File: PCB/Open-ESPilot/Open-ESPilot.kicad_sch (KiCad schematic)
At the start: 0 parts

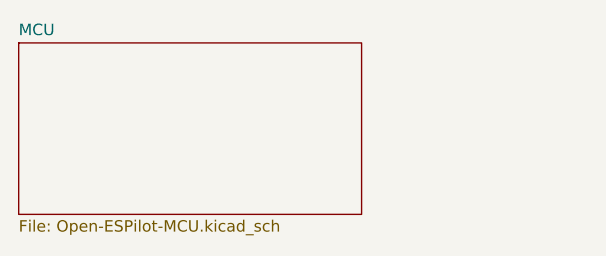
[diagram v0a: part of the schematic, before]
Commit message: Finished schematic for the ESP32S3.
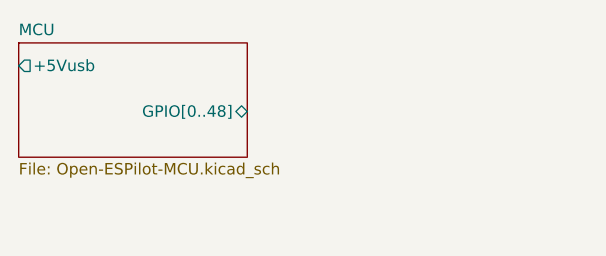
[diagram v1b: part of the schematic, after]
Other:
- sheet MCU ports: added +5Vusb, GPIO[0..48]; removed none
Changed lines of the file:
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@@
 	(sheet
 		(at 110.49 77.47)
-		(size 38.1 19.05)
+		(size 25.4 12.7)
 		(exclude_from_sim no)
 		(in_bom yes)
@@
 		)
 		(property "Sheetfile" "Open-ESPilot-MCU.kicad_sch"
-			(at 110.49 97.1046 0)
+			(at 110.49 90.7546 0)
 			(effects
 				(font
@@
 			)
 		)
+		(pin "+5Vusb" output
+			(at 110.49 80.01 180)
+			(effects
+				(font
+					(size 1.27 1.27)
+				)
+				(justify left)
+			)
+		)
+		(pin "GPIO[0..48]" bidirectional
+			(at 135.89 85.09 0)
+			(effects
+				(font
+					(size 1.27 1.27)
+				)
+				(justify right)
+			)
+		)

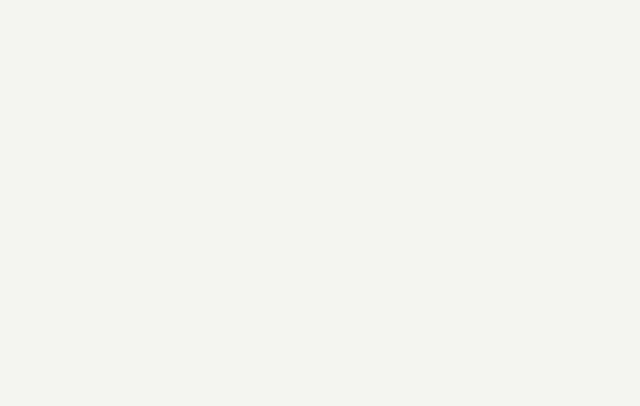
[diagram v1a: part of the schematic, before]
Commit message: Edited the MP1584 module and added Schematic and footprint of the GY-91 and implemented it to the schematic.
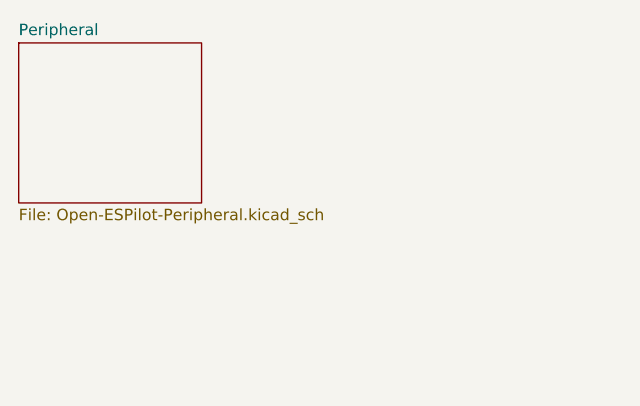
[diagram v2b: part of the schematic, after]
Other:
- added sheet Peripheral (Open-ESPilot-Peripheral.kicad_sch)
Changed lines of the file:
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@@
+		)
+	)
+	(sheet
+		(at 52.07 29.21)
+		(size 20.32 17.78)
+		(exclude_from_sim no)
+		(in_bom yes)
+		(on_board yes)
+		(dnp no)
+		(fields_autoplaced yes)
+		(stroke
+			(width 0.1524)
+			(type solid)
+		)
+		(fill
+			(color 0 0 0 0.0000)
+		)
+		(property "Sheetname" "Peripheral"
+			(at 52.07 28.4984 0)
+			(effects
+				(font
+					(size 1.27 1.27)
+				)
+				(justify left bottom)
+			)
+		)
+		(property "Sheetfile" "Open-ESPilot-Peripheral.kicad_sch"
+			(at 52.07 47.5746 0)
+			(effects
+				(font
+					(size 1.27 1.27)
+				)
+				(justify left top)
+			)
+		)
+		(instances
+			(project "Open-ESPilot"
+				(path "/2992e60d-a645-4cd7-90ae-fe72311b6bee"
+					(page "4")
+				)
+			)
 		)
 	)

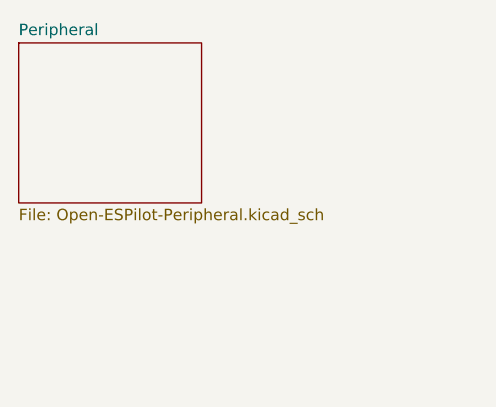
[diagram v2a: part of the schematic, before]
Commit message: Edited Pin definitions to Open ESPilot. And added the pheripherials to the schematic. Also new journal entry.
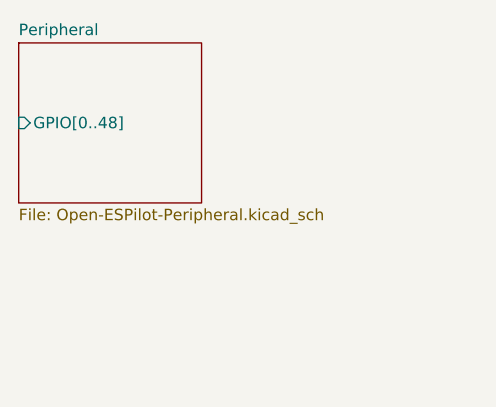
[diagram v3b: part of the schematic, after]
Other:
- sheet Peripheral ports: added GPIO[0..48]; removed none
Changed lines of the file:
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@@
+			)
+		)
+		(pin "GPIO[0..48]" input
+			(at 52.07 38.1 180)
+			(effects
+				(font
+					(size 1.27 1.27)
+				)
+				(justify left)
 			)
 		)

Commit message: Schematic Fixes
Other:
- sheet Peripheral ports: added ADC-Voltage, SCL, SDA; removed none
- sheet Power ports: added +5Vusb, ADC-Voltage, SCL, SDA; removed none
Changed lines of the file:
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@@
 		(title "Open-ESPilot")
 	)
+	(bus
+		(pts
+			(xy 162.56 91.44) (xy 167.64 91.44)
+		)
+		(stroke
+			(width 0)
+			(type default)
+		)
+	)
+	(wire
+		(pts
+			(xy 88.9 116.84) (xy 176.53 116.84)
+		)
+		(stroke
+			(width 0)
+			(type default)
+		)
+	)
+	(wire
+		(pts
+			(xy 116.84 83.82) (xy 121.92 83.82)
+		)
+		(stroke
+			(width 0)
+			(type default)
+		)
+	)
+	(wire
+		(pts
+			(xy 179.07 119.38) (xy 179.07 109.22)
+		)
+		(stroke
+			(width 0)
+			(type default)
+		)
+	)
+	(wire
+		(pts
+			(xy 85.09 114.3) (xy 172.72 114.3)
+		)
+		(stroke
+			(width 0)
+			(type default)
+		)
+	)
+	(wire
+		(pts
+			(xy 91.44 109.22) (xy 91.44 119.38)
+		)
+		(stroke
+			(width 0)
+			(type default)
+		)
+	)
+	(wire
+		(pts
+			(xy 91.44 119.38) (xy 179.07 119.38)
+		)
+		(stroke
+			(width 0)
+			(type default)
+		)
+	)
+	(wire
+		(pts
+			(xy 85.09 109.22) (xy 85.09 114.3)
+		)
+		(stroke
+			(width 0)
+			(type default)
+		)
+	)
+	(wire
+		(pts
+			(xy 88.9 109.22) (xy 88.9 116.84)
+		)
+		(stroke
+			(width 0)
+			(type default)
+		)
+	)
+	(wire
+		(pts
+			(xy 172.72 114.3) (xy 172.72 109.22)
+		)
+		(stroke
+			(width 0)
+			(type default)
+		)
+	)
+	(wire
+		(pts
+			(xy 176.53 116.84) (xy 176.53 109.22)
+		)
+		(stroke
+			(width 0)
+			(type default)
+		)
+	)
 	(sheet
-		(at 176.53 77.47)
-		(size 33.02 17.78)
+		(at 80.01 80.01)
+		(size 36.83 29.21)
 		(exclude_from_sim no)
 		(in_bom yes)
@@
 		)
 		(property "Sheetname" "Power"
-			(at 176.53 76.7584 0)
+			(at 80.01 79.2984 0)
 			(effects
 				(font
@@
 		)
 		(property "Sheetfile" "Open-ESPilot-Power.kicad_sch"
-			(at 176.53 95.8346 0)
+			(at 80.01 109.8046 0)
 			(effects
 				(font
@@
 				)
 				(justify left top)
+			)
+		)
+		(pin "+5Vusb" input
+			(at 116.84 83.82 0)
+			(effects
+				(font
+					(size 1.27 1.27)
+				)
+				(justify right)
+			)
+		)
+		(pin "ADC-Voltage" output
+			(at 85.09 109.22 270)
+			(effects
+				(font
+					(size 1.27 1.27)
+				)
+				(justify left)
+			)
+		)
+		(pin "SCL" bidirectional
+			(at 88.9 109.22 270)
+			(effects
+				(font
+					(size 1.27 1.27)
+				)
+				(justify left)
+			)
+		)
+		(pin "SDA" bidirectional
+			(at 91.44 109.22 270)
+			(effects
+				(font
+					(size 1.27 1.27)
+				)
+				(justify left)
 			)
 		)
@@
 	)
 	(sheet
-		(at 110.49 77.47)
-		(size 25.4 12.7)
+		(at 121.92 80.01)
+		(size 40.64 29.21)
 		(exclude_from_sim no)
 		(in_bom yes)
@@
 		)
 		(property "Sheetname" "MCU"
-			(at 110.49 76.7584 0)
+			(at 121.92 79.2984 0)
 			(effects
 				(font
@@
 		)
 		(property "Sheetfile" "Open-ESPilot-MCU.kicad_sch"
-			(at 110.49 90.7546 0)
+			(at 121.92 109.8046 0)
 			(effects
 				(font
@@
 		)
 		(pin "+5Vusb" output
-			(at 110.49 80.01 180)
+			(at 121.92 83.82 180)
 			(effects
 				(font
@@
 		)
 		(pin "GPIO[0..48]" bidirectional
-			(at 135.89 85.09 0)
+			(at 162.56 91.44 0)
 			(effects
 				(font
@@
 	)
 	(sheet
-		(at 52.07 29.21)
-		(size 20.32 17.78)
+		(at 167.64 80.01)
+		(size 40.64 29.21)
 		(exclude_from_sim no)
 		(in_bom yes)
@@
 		)
 		(property "Sheetname" "Peripheral"
-			(at 52.07 28.4984 0)
+			(at 167.64 79.2984 0)
 			(effects
 				(font
@@
 		)
 		(property "Sheetfile" "Open-ESPilot-Peripheral.kicad_sch"
-			(at 52.07 47.5746 0)
+			(at 167.64 109.8046 0)
 			(effects
 				(font
@@
 		)
 		(pin "GPIO[0..48]" input
-			(at 52.07 38.1 180)
-			(effects
-				(font
+			(at 167.64 91.44 180)
+			(effects
+				(font
+					(size 1.27 1.27)
+				)
+				(justify left)
+			)
+		)
+		(pin "ADC-Voltage" input
+			(at 172.72 109.22 270)
+			(effects
+				(font
+					(size 1.27 1.27)
+				)
+				(justify left)
+			)
+		)
+		(pin "SCL" bidirectional
+			(at 176.53 109.22 270)
+			(effects
+				(font
+					(size 1.27 1.27)
+				)
+				(justify left)
+			)
+		)
+		(pin "SDA" bidirectional
+			(at 179.07 109.22 270)
+			(effects
+				(font

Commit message: more Schematic fixes yay
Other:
- sheet MCU ports: added +3V3; removed none
- sheet Peripheral ports: added +3V3, +5V; removed none
- sheet Power ports: added +3V3, +5V; removed none

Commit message: in dabenginging of V1.1
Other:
- sheet Peripheral ports: added +5Vreg; removed none
- sheet Power ports: added +5Vreg; removed none
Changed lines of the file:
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@@
 	(title_block
 		(title "Open-ESPilot")
+		(rev "V1.1")
 	)
 	(wire
@@
 	(wire
 		(pts
-			(xy 99.06 77.47) (xy 99.06 80.01)
+			(xy 96.52 77.47) (xy 96.52 80.01)
+		)
+		(stroke
+			(width 0)
+			(type default)
+		)
+	)
+	(wire
+		(pts
+			(xy 104.14 77.47) (xy 104.14 80.01)
 		)
 		(stroke
@@
 	(wire
 		(pts
-			(xy 91.44 77.47) (xy 91.44 80.01)
+			(xy 88.9 77.47) (xy 88.9 80.01)
 		)
 		(stroke
@@
 	(wire
 		(pts
+			(xy 191.77 77.47) (xy 191.77 80.01)
+		)
+		(stroke
+			(width 0)
+			(type default)
+		)
+	)
+	(wire
+		(pts
 			(xy 85.09 109.22) (xy 85.09 114.3)
 		)
@@
 	(wire
 		(pts
-			(xy 189.23 77.47) (xy 189.23 80.01)
+			(xy 203.2 77.47) (xy 203.2 80.01)
 		)
 		(stroke
@@
 	(symbol
 		(lib_id "power:+5V")
-		(at 99.06 77.47 0)
+		(at 104.14 77.47 0)
 		(unit 1)
 		(exclude_from_sim no)
@@
 		(fields_autoplaced yes)
 		(property "Reference" "#PWR02"
-			(at 99.06 81.28 0)
+			(at 104.14 81.28 0)
 			(effects
 				(font
@@
 		)
 		(property "Value" "+5V"
-			(at 99.06 72.39 0)
+			(at 104.14 72.39 0)
 			(effects
 				(font
@@
 		)
 		(property "Footprint" ""
-			(at 99.06 77.47 0)
+			(at 104.14 77.47 0)
 			(effects
 				(font
@@
 		)
 		(property "Datasheet" ""
-			(at 99.06 77.47 0)
+			(at 104.14 77.47 0)
 			(effects
 				(font
@@
 		)
 		(property "Description" "Power symbol creates a global label with name \"+5V\""
-			(at 99.06 77.47 0)
+			(at 104.14 77.47 0)
 			(effects
 				(font
@@
 	(symbol
 		(lib_id "power:+5V")
-		(at 189.23 77.47 0)
+		(at 203.2 77.47 0)
 		(unit 1)
 		(exclude_from_sim no)
@@
 		(fields_autoplaced yes)
 		(property "Reference" "#PWR05"
-			(at 189.23 81.28 0)
+			(at 203.2 81.28 0)
 			(effects
 				(font
@@
 		)
 		(property "Value" "+5V"
-			(at 189.23 72.39 0)
+			(at 203.2 72.39 0)
 			(effects
 				(font
@@
 		)
 		(property "Footprint" ""
-			(at 189.23 77.47 0)
+			(at 203.2 77.47 0)
 			(effects
 				(font
@@
 		)
 		(property "Datasheet" ""
-			(at 189.23 77.47 0)
+			(at 203.2 77.47 0)
 			(effects
 				(font
@@
 		)
 		(property "Description" "Power symbol creates a global label with name \"+5V\""
-			(at 189.23 77.47 0)
+			(at 203.2 77.47 0)
 			(effects
 				(font
@@
 		)
 		(instances
-			(project ""
+			(project "Open-ESPilot"
 				(path "/2992e60d-a645-4cd7-90ae-fe72311b6bee"
 					(reference "#PWR05")
@@
 	)
 	(symbol
+		(lib_id "power:+5V")
+		(at 96.52 77.47 0)
+		(unit 1)
+		(exclude_from_sim no)
+		(in_bom yes)
+		(on_board yes)
+		(dnp no)
+		(fields_autoplaced yes)
+		(property "Reference" "#PWR041"
+			(at 96.52 81.28 0)
+			(effects
+				(font
+					(size 1.27 1.27)
+				)
+				(hide yes)
+			)
+		)
+		(property "Value" "+5Vreg"
+			(at 96.52 72.39 0)
+			(effects
+				(font
+					(size 1.27 1.27)
+				)
+			)
+		)
+		(property "Footprint" ""
+			(at 96.52 77.47 0)
+			(effects
+				(font
+					(size 1.27 1.27)
+				)
+				(hide yes)
+			)
+		)
+		(property "Datasheet" ""
+			(at 96.52 77.47 0)
+			(effects
+				(font
+					(size 1.27 1.27)
+				)
+				(hide yes)
+			)
+		)
+		(property "Description" "Power symbol creates a global label with name \"+5V\""
+			(at 96.52 77.47 0)
+			(effects
+				(font
+					(size 1.27 1.27)
+				)
+				(hide yes)
+			)
+		)
+		(pin "1"
+		)
+		(instances
+			(project "Open-ESPilot"
+				(path "/2992e60d-a645-4cd7-90ae-fe72311b6bee"
+					(reference "#PWR041")
+					(unit 1)
+				)
+			)
+		)
+	)
+	(symbol
 		(lib_id "power:+3V3")
-		(at 91.44 77.47 0)
+		(at 88.9 77.47 0)
 		(unit 1)
 		(exclude_from_sim no)
@@
 		(fields_autoplaced yes)
 		(property "Reference" "#PWR01"
-			(at 91.44 81.28 0)
+			(at 88.9 81.28 0)
 			(effects
 				(font
@@
 		)
 		(property "Value" "+3V3"
-			(at 91.44 72.39 0)
+			(at 88.9 72.39 0)
 			(effects
 				(font
@@
 		)
 		(property "Footprint" ""
-			(at 91.44 77.47 0)
+			(at 88.9 77.47 0)
 			(effects
 				(font
@@
 		)
 		(property "Datasheet" ""
-			(at 91.44 77.47 0)
+			(at 88.9 77.47 0)
 			(effects
 				(font
@@
 		)
 		(property "Description" "Power symbol creates a global label with name \"+3V3\""
-			(at 91.44 77.47 0)
+			(at 88.9 77.47 0)
 			(effects
 				(font
@@
 	)
 	(symbol
+		(lib_id "power:+5V")
+		(at 191.77 77.47 0)
+		(unit 1)
+		(exclude_from_sim no)
+		(in_bom yes)
+		(on_board yes)
+		(dnp no)
+		(fields_autoplaced yes)
+		(property "Reference" "#PWR057"
+			(at 191.77 81.28 0)
+			(effects
+				(font
+					(size 1.27 1.27)
+				)
+				(hide yes)
+			)
+		)
+		(property "Value" "+5Vreg"
+			(at 191.77 72.39 0)
+			(effects
+				(font
+					(size 1.27 1.27)
+				)
+			)
+		)
+		(property "Footprint" ""
+			(at 191.77 77.47 0)
+			(effects
+				(font
+					(size 1.27 1.27)
+				)
+				(hide yes)
+			)
+		)
+		(property "Datasheet" ""
+			(at 191.77 77.47 0)
+			(effects
+				(font
+					(size 1.27 1.27)
+				)
+				(hide yes)
+			)
+		)
+		(property "Description" "Power symbol creates a global label with name \"+5V\""
+			(at 191.77 77.47 0)
+			(effects
+				(font
+					(size 1.27 1.27)
+				)
+				(hide yes)
+			)
+		)
+		(pin "1"
+		)
+		(instances
+			(project "Open-ESPilot"
+				(path "/2992e60d-a645-4cd7-90ae-fe72311b6bee"
+					(reference "#PWR057")
+					(unit 1)
+				)
+			)
+		)
+	)
+	(symbol
 		(lib_id "power:+3V3")
 		(at 134.62 77.47 0)
@@
 		)
 		(instances
-			(project ""
+			(project "Open-ESPilot"
 				(path "/2992e60d-a645-4cd7-90ae-fe72311b6bee"
 					(reference "#PWR03")
@@
 		)
 		(pin "+3V3" output
-			(at 91.44 80.01 90)
+			(at 88.9 80.01 90)
 			(effects
 				(font
@@
 		)
 		(pin "+5V" output
-			(at 99.06 80.01 90)
+			(at 104.14 80.01 90)
+			(effects
+				(font
+					(size 1.27 1.27)
+				)
+				(justify right)
+			)
+		)
+		(pin "+5Vreg" output
+			(at 96.52 80.01 90)
 			(effects
 				(font
@@
 		)
 		(pin "+5V" input
-			(at 189.23 80.01 90)
-			(effects
-				(font
+			(at 203.2 80.01 90)
+			(effects
+				(font
+					(size 1.27 1.27)
+				)
+				(justify right)
+			)
+		)
+		(pin "+5Vreg" input
+			(at 191.77 80.01 90)
+			(effects
+				(font
